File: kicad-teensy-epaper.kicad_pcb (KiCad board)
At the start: 2 copper layers, 78.8 x 57.3 mm, 21 parts, among them J1 TEENSY3.2-72MHz, J2 HEADER-FEMALE-34POS-FFC-SMT-1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, Q1 Q_NMOS_GDS

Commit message: Reworked layout for aesthetics
OSH Park order m5ay7bby on May 4th, 2017.
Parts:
- J1: value TEENSY3.2-72MHz -> TEENSY3.2-72MHz-SIMPLE; footprint Wickerlib:TEENSY-3.2-SILK -> Wickerlib:TEENSY-3.2-SILK-SIMPLE
- moved C1 4.78 mm to (105.9, 40.6)
- moved CAP2 3.19 mm to (138.2, 63.8)
- moved CAP1 3.18 mm to (138.2, 48.7)
- moved A 3.16 mm to (138.2, 78.8)
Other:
- board size 78.8 x 57.3 mm -> 83.4 x 57.2 mm
- board text added: "#"
- board text added: "*"
- board text added: "+"
- board text added: "2017-05-04"
- board text added: "github.com/pdp7/kicad-teensy-epaper"
- board text added: "github.com/pdp7/kicad-teensy-epaper Drew Fustini <drew@oshpark.com>"
- board text removed: "2017-04-24"
- board text removed: "A"
- board text removed: "B"
- board text removed: "C"
- board text removed: "https://github.com/pdp7/kicad-teensy-epaper"

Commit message: Set pad soldermask clearance to 0
The display fine pitch connector footprint
does not have solder mask between the pads.

Chris Boros advised I could have solder mask
between the pads by setting the clearance to 0.
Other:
- rule pad_to_mask_clearance: 0.0762 -> 0
- rule solder_mask_min_width: 0.1016 -> 0.0762
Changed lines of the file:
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@@
     (pad_size 10.16 10.16)
     (pad_drill 0)
-    (pad_to_mask_clearance 0.0762)
-    (solder_mask_min_width 0.1016)
+    (pad_to_mask_clearance 0)
+    (solder_mask_min_width 0.0762)
     (pad_to_paste_clearance -0.0762)
     (aux_axis_origin 196.5452 123.5456)

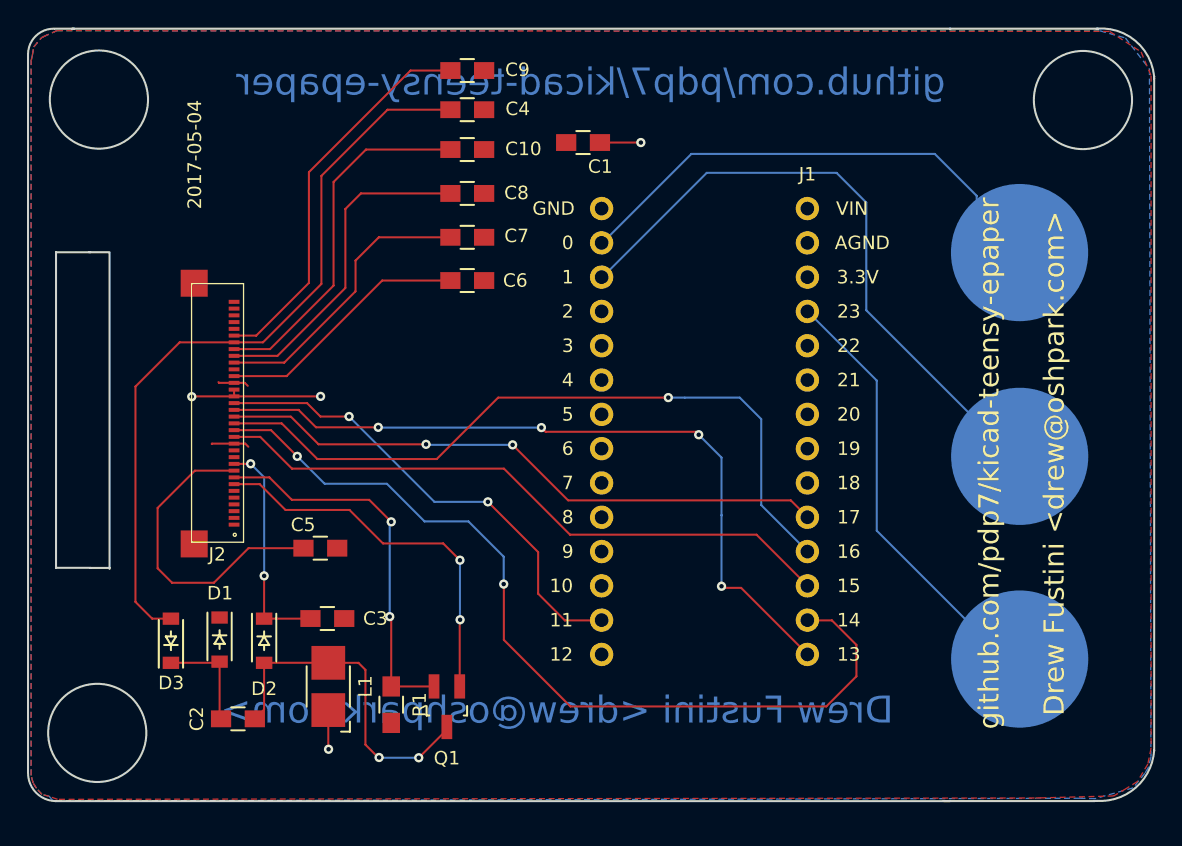
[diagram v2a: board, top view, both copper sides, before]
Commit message: add JST connector for lipo battery
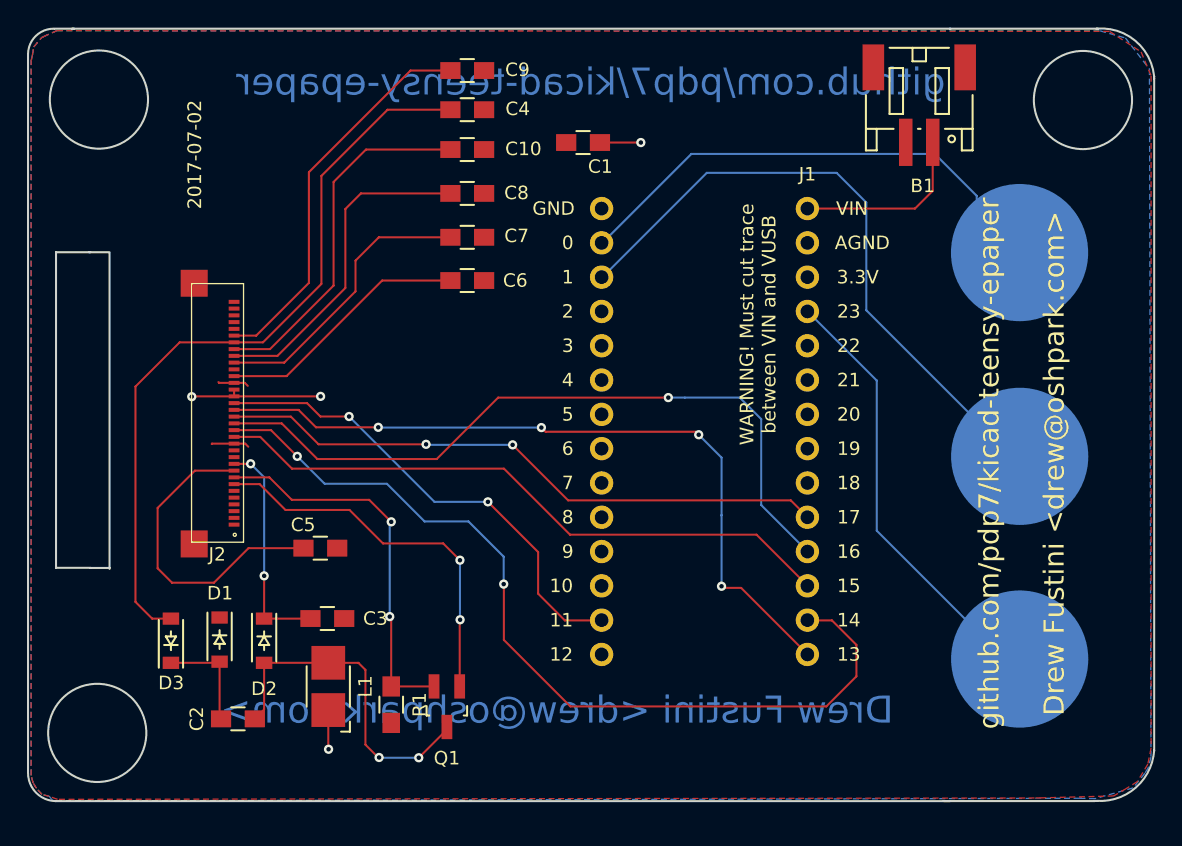
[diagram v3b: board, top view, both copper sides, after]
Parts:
- added B1: BATT-LIPO-3.7V-150MAH-JST-2PIN, Wickerlib:CONN-JST-S2B-PH-SM4-TB, F.Cu at (130.8, 37.8)
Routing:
- net Net-(B1-Pad1): track 0.00 -> 13.4 mm
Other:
- board text added: "2017-07-02"
- board text added: "WARNING! Must cut trace between VIN and VUSB"
- board text removed: "2017-05-04"
